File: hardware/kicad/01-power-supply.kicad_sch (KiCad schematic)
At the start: 29 parts, among them J1 USB_C, J3 JST PH 2-pin, Q1 SI2301CDS, SW16 SS-12D00G3, U2 IP5306, U3 SY8089AAAC, U4 USBLC6-2SC6

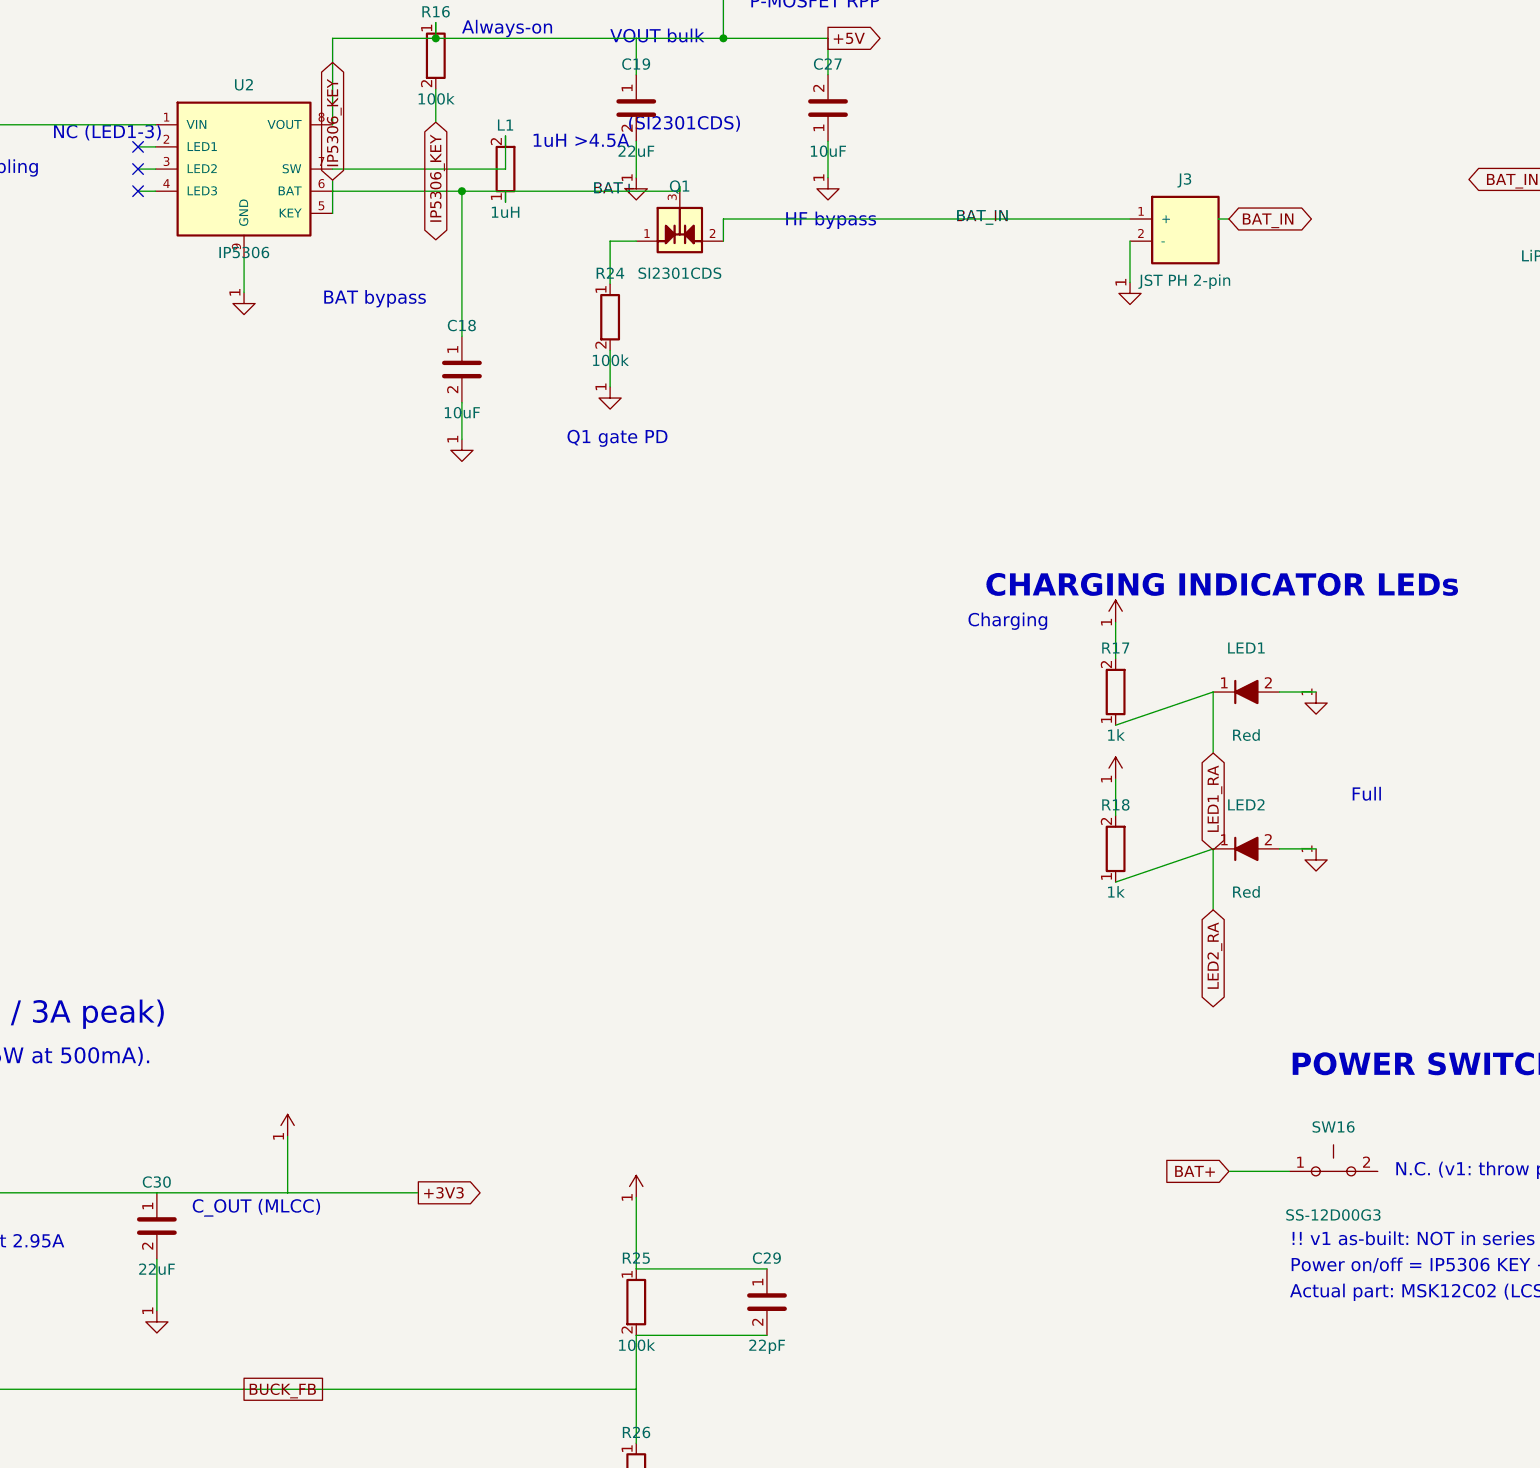
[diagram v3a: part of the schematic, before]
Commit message: fix(schematics): first clean ERC — uuid collisions, instance paths, C3 float
The first-ever ERC run (unlocked by the SW ref rename) reported errors
on geometrically perfect cells while skipping their identical twins.
Root causes, both in generate_schematics:

1. Cross-sheet uuid collisions — every sheet's context counted 1,2,3...
   into the same "{n}-cafe-4000-8000-{n}" pattern, so the same uuid
   lived in several files. ERC merged unrelated objects across sheets:
   phantom "pin not connected" findings, wrong-sheet attribution, and
   pins silently DROPPED from the exported netlist (L1.2/U2.7/Q1.1/
   R24.1 did not exist, which is why netlist-diff T4 "passed"). uuids
   now carry a per-file namespace nibble in the variant group.
2. Single-level symbol instance paths ("/<sheet-uuid>") — loaders fell
   back to "the first instance" (KiBot W182). Both accepted shapes are
   now emitted; KiCad's netlister and ERC resolve different ones.

Real findings fixed once the phantoms cleared:
- C3 (ESP32 decoupling): its +3V3 tap wire ended in the gap between the
  +3V3 wire (ends x=184.76) and the LCD_CS stub (starts x=215.24) —
  floating, one step from a drawn +3V3/LCD_CS short. Moved between C4
  and the module edge, junction added, caption moved off C26.
- SW16 pin 2: explicit no_connect (throw side deliberately unrouted on
  v1 — see project_swpwr memory).
- PWR_FLAG on +3V3 and GND (+5V must NOT get one: IP5306 VOUT is
  power_out). LX and RPP_GATE now labelled with the PCB's net names;
  both closed out of verify_netlist_diff T2_ALLOW — two more nodes the
  cross-check actually verifies.

New standing gate: scripts/verify_erc.py (make verify-erc) — KiCad ERC
at error severity, in VERIFY_ALL_SCRIPTS, routed by the existing `erc`
law (pcb-engineer, dead-board), proven by mutation (deleting C3's
junction turns it red). .claudeheavy covers the new KiBot ERC/DRC JSON
reports and ESP-IDF managed_components.

Not gated on purpose: 651 warning-severity ERC findings (endpoint_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
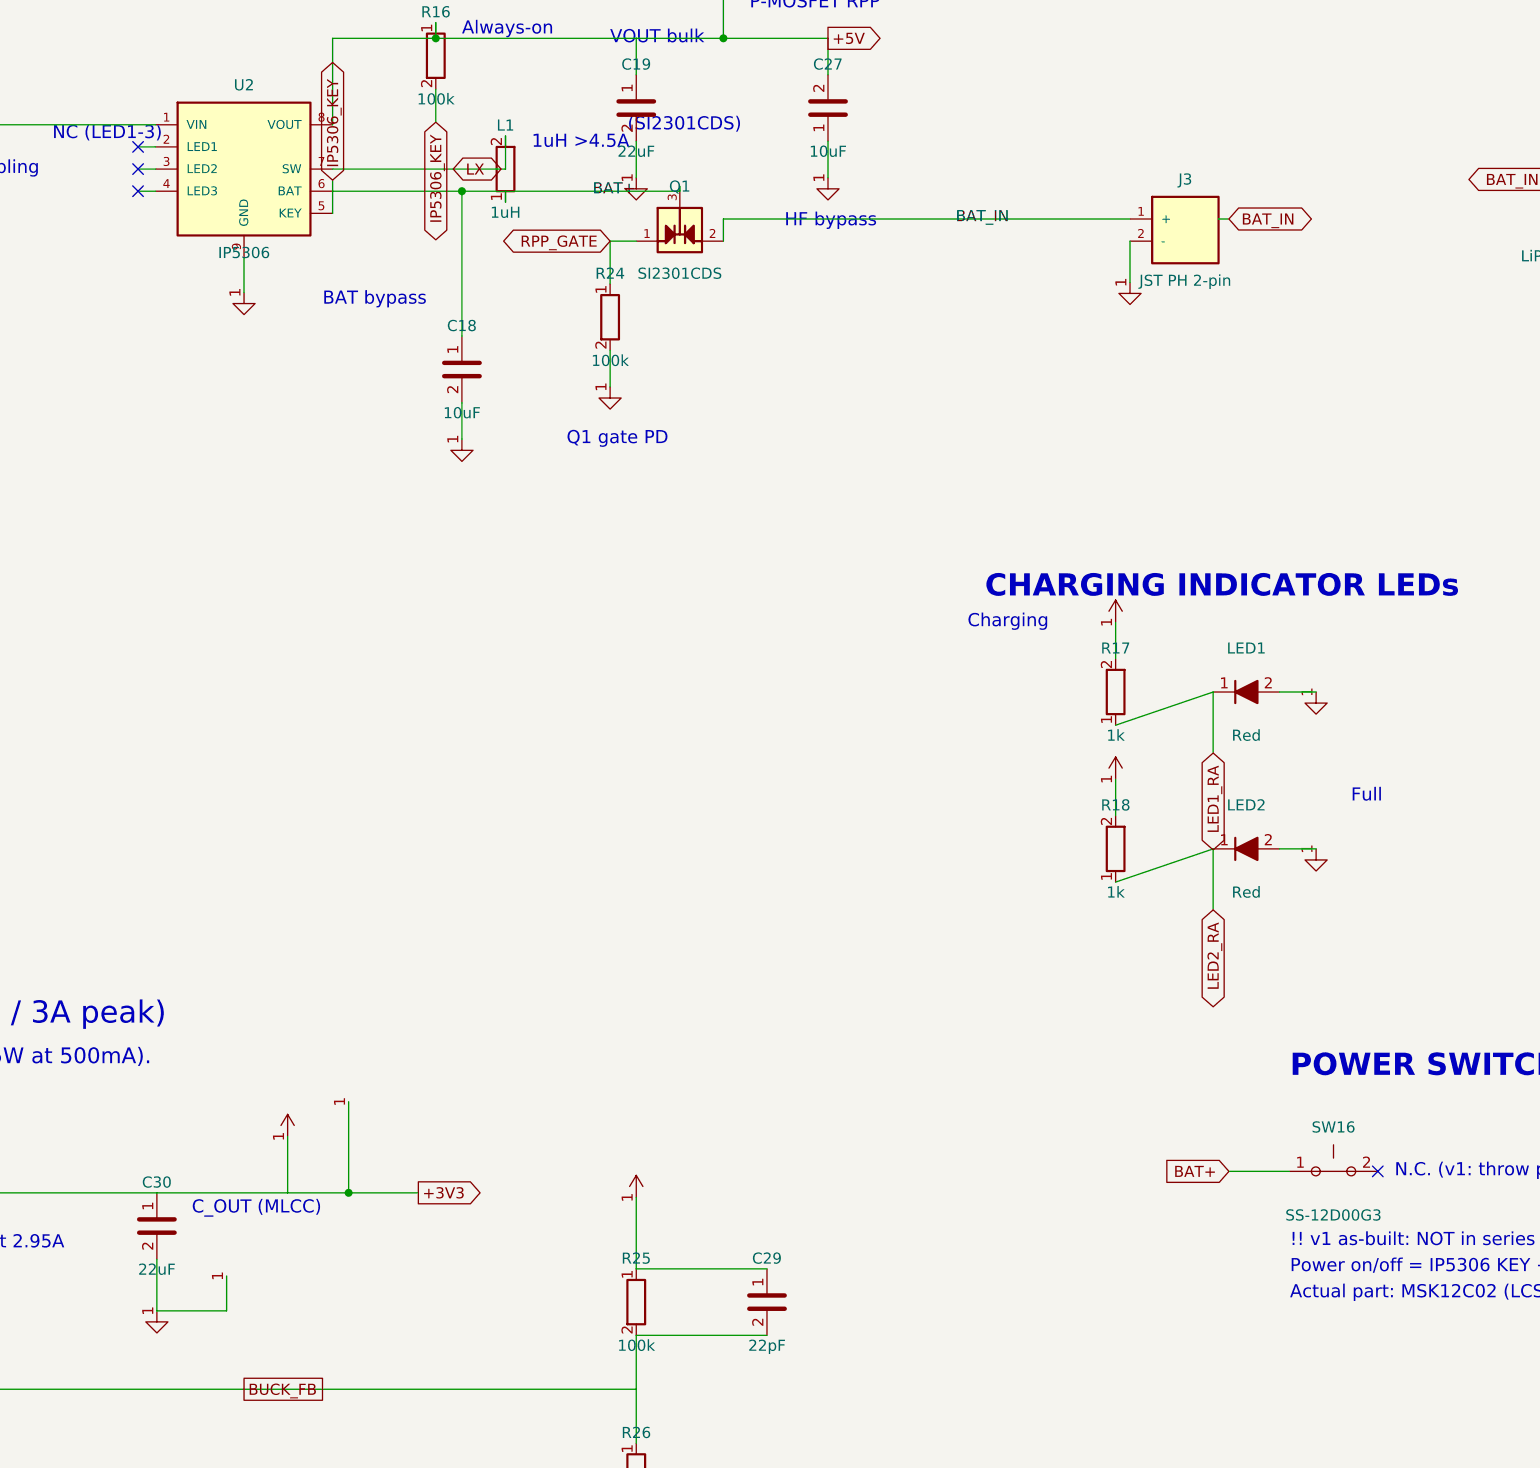
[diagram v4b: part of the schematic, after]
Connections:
- net LX: now reaches L1.2, U2.7 (SW)
- net RPP_GATE: now reaches Q1.1, R24.1
- no-connect marks 3 -> 4

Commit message: refactor(schematics): zero dead nets, T1_ALLOW empty, legacy AMS1117 removed
Dead-net sweep requested by the user, both sides checked:

- PCB: already clean — 54 declared nets, 54 carrying copper (ORPHAN
  e-test gate enforces it). Nothing to do.
- Schematic: the five one-pin "GPIOnn" phantom nets (GPIO15/16/35/36/37)
  are now explicit no_connect markers. GPIO35-37 are the WROOM-1
  on-module PSRAM pins that MUST stay externally unconnected; 15/16 were
  freed when audio went PDM-DOUT-only (R10-LOW-2). T1_ALLOW is now
  EMPTY — five more allowlist holes closed, after LX/RPP_GATE earlier
  today: seven total, each one a node the schematic<->PCB cross-check
  now actually compares.
- Dangling BAT_IN stub next to J3 deleted: its wire started at
  jst_x+3.81 where J3 has no pin (both pins are on the connector's left
  side) — flagged by ERC as unconnected_wire_endpoint since forever.
- VBUS / BAT+ / BAT_IN no longer mix local and global labels on one net
  (ERC same_local_global_label): global labels only, so net merging no
  longer relies on KiCad's same-text courtesy.
- lib_symbols: legacy AMS1117-3.3 symbol removed (unused since the
  SY8089 swap; its stray power_out pins were noise in pin-type audits).

Docs: ecosystem-analysis updated (dead-net sweep + empty T1_ALLOW).
Deferred deep-dives recorded in memory: SW16 shell-isolation datasheet
check, 636 remaining ERC warnings, netlist cosmetic warning.

Tests: verify-all 80/80, verify-erc PASS (0 errors; warnings 651->636),
netlist-diff 4/4 with T1_ALLOW=∅, overlaps 651 items clean,
label-attach 131/131, verify-memory 6/6, website-build green.
Schematic SVG/PDF renders + combined PDF regenerated.

Co-Authored-By: Claude Fable 5 <noreply@anthropic.com>
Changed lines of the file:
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@@
   (symbol (lib_id "IP5306") (at 160 85 0) (unit 1) (exclude_from_sim no) (in_bom yes) (on_board yes) (dnp no) (property "Reference" "U2" (at 160 75.38 0) (effects (font (size 1.27 1.27)))) (property "Value" "IP5306" (at 160 94.62 0) (effects (font (size 1.27 1.27)))) (pin "1") (pin "2") (pin "3") (pin "4") (pin "5") (pin "6") (pin "7") (pin "8") (pin "9") (instances (project "esp32-emu-turbo" (path "/00000002-cafe-4000-8000-000000000002" (reference "U2") (unit 1)) (path "/00000001-cafe-4000-8000-000000000001/00000002-cafe-4000-8000-000000000002" (reference "U2") (unit 1)))))
   (wire (pts (xy 57.62 81.19) (xy 118 81.19)) (stroke (width 0) (type default)))
-  (label "VBUS" (at 62.62 81.19 0) (effects (font (size 1.27 1.27))))
+  (global_label "VBUS" (shape bidirectional) (at 62.62 81.19 0) (effects (font (size 1.27 1.27))) (property "Intersheetrefs" "" (at 0 0 0) (effects (font (size 1.27 1.27)) hide)))
   (wire (pts (xy 118 81.19) (xy 118 86.19)) (stroke (width 0) (type default)))
   (symbol (lib_id "C") (at 118 90 0) (unit 1) (exclude_from_sim no) (in_bom yes) (on_board yes) (dnp no) (property "Reference" "C17" (at 118 85.0 0) (effects (font (size 1.27 1.27)))) (property "Value" "10uF" (at 118 95.0 0) (effects (font (size 1.27 1.27)))) (pin "1") (pin "2") (instances (project "esp32-emu-turbo" (path "/00000002-cafe-4000-8000-000000000002" (reference "C17") (unit 1)) (path "/00000001-cafe-4000-8000-000000000001/00000002-cafe-4000-8000-000000000002" (reference "C17") (unit 1)))))
@@
   (junction (at 185 87.54) (diameter 0) (color 0 0 0 0))
   (wire (pts (xy 210 87.54) (xy 210 87)) (stroke (width 0) (type default)))
-  (label "BAT+" (at 200 87.54 0) (effects (font (size 1.27 1.27))))
+  (global_label "BAT+" (shape bidirectional) (at 200 87.54 180) (effects (font (size 1.27 1.27))) (property "Intersheetrefs" "" (at 0 0 0) (effects (font (size 1.27 1.27)) hide)))
   (wire (pts (xy 215 93.27) (xy 215 90.73)) (stroke (width 0) (type default)))
   (wire (pts (xy 215 90.73) (xy 261.65 90.73)) (stroke (width 0) (type default)))
-  (label "BAT_IN" (at 241.64999999999998 90.73 0) (effects (font (size 1.27 1.27))))
+  (global_label "BAT_IN" (shape bidirectional) (at 241.64999999999998 90.73 0) (effects (font (size 1.27 1.27))) (property "Intersheetrefs" "" (at 0 0 0) (effects (font (size 1.27 1.27)) hide)))
   (symbol (lib_id "R") (at 202 102 0) (unit 1) (exclude_from_sim no) (in_bom yes) (on_board yes) (dnp no) (property "Reference" "R24" (at 202 97.0 0) (effects (font (size 1.27 1.27)))) (property "Value" "100k" (at 202 107.0 0) (effects (font (size 1.27 1.27)))) (pin "1") (pin "2") (instances (project "esp32-emu-turbo" (path "/00000002-cafe-4000-8000-000000000002" (reference "R24") (unit 1)) (path "/00000001-cafe-4000-8000-000000000001/00000002-cafe-4000-8000-000000000002" (reference "R24") (unit 1)))))
   (text "Q1 gate PD" (at 197 116 0) (effects (font (size 1.5 1.5)) (justify left)))
@@
   (text "105080" (at 320 87 0) (effects (font (size 1.5 1.5)) (justify left)))
   (text "3.7V 5000mAh" (at 320 91 0) (effects (font (size 1.5 1.5)) (justify left)))
-  (global_label "BAT_IN" (shape bidirectional) (at 273 90.73 0) (effects (font (size 1.27 1.27))) (property "Intersheetrefs" "" (at 0 0 0) (effects (font (size 1.27 1.27)) hide)))
-  (wire (pts (xy 271.81 90.73) (xy 273 90.73)) (stroke (width 0) (type default)))
   (global_label "BAT_IN" (shape bidirectional) (at 310 86.19 180) (effects (font (size 1.27 1.27))) (property "Intersheetrefs" "" (at 0 0 0) (effects (font (size 1.27 1.27)) hide)))
   (wire (pts (xy 310 86.19) (xy 315 86.19)) (stroke (width 0) (type default)))
